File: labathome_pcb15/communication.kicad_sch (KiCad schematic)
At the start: 19 parts, among them M1 W5500_mini, SW2 OFF TERM ON, SW3 TERM ON, U1 MAX3485, U15 NRF24L01, U6 RFM95W-868S2, U7 SN65HVD230, X3 SIM7080G

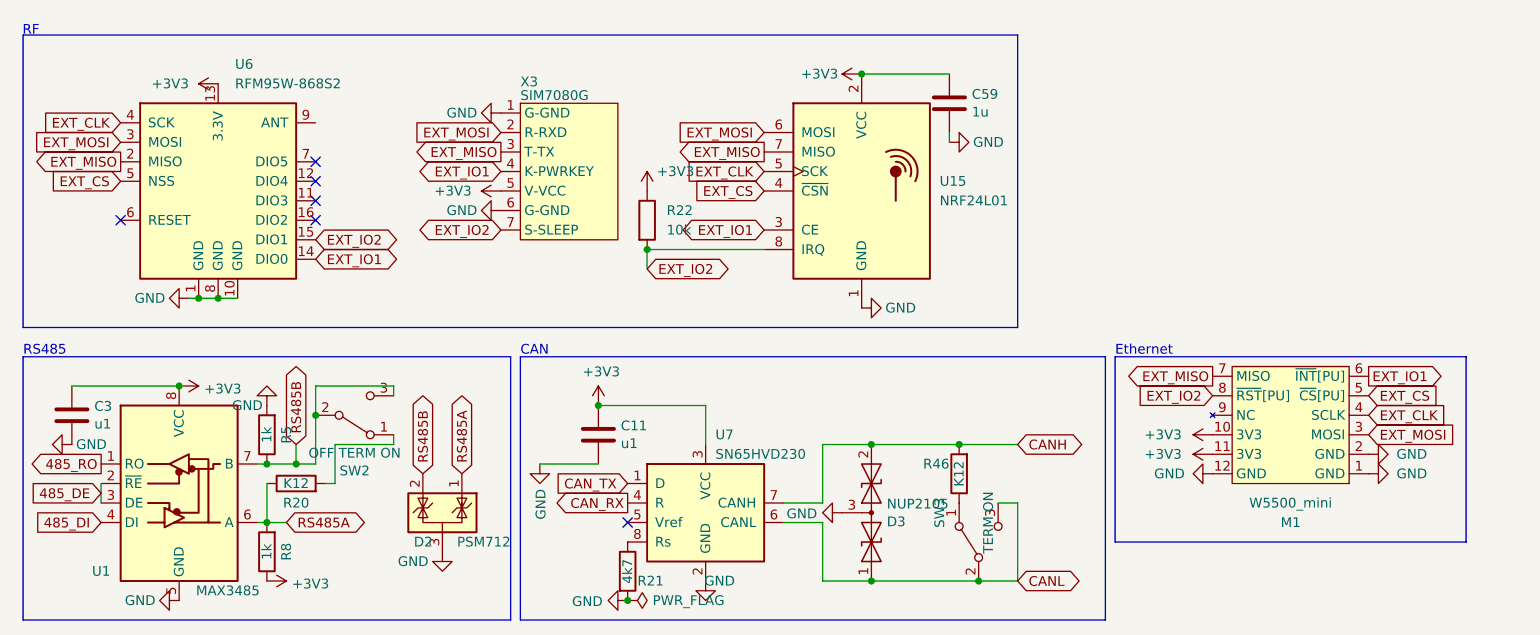
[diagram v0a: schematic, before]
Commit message: Various PCB and Code updates after review from Jana Marie Hemsing. Big Thankyou
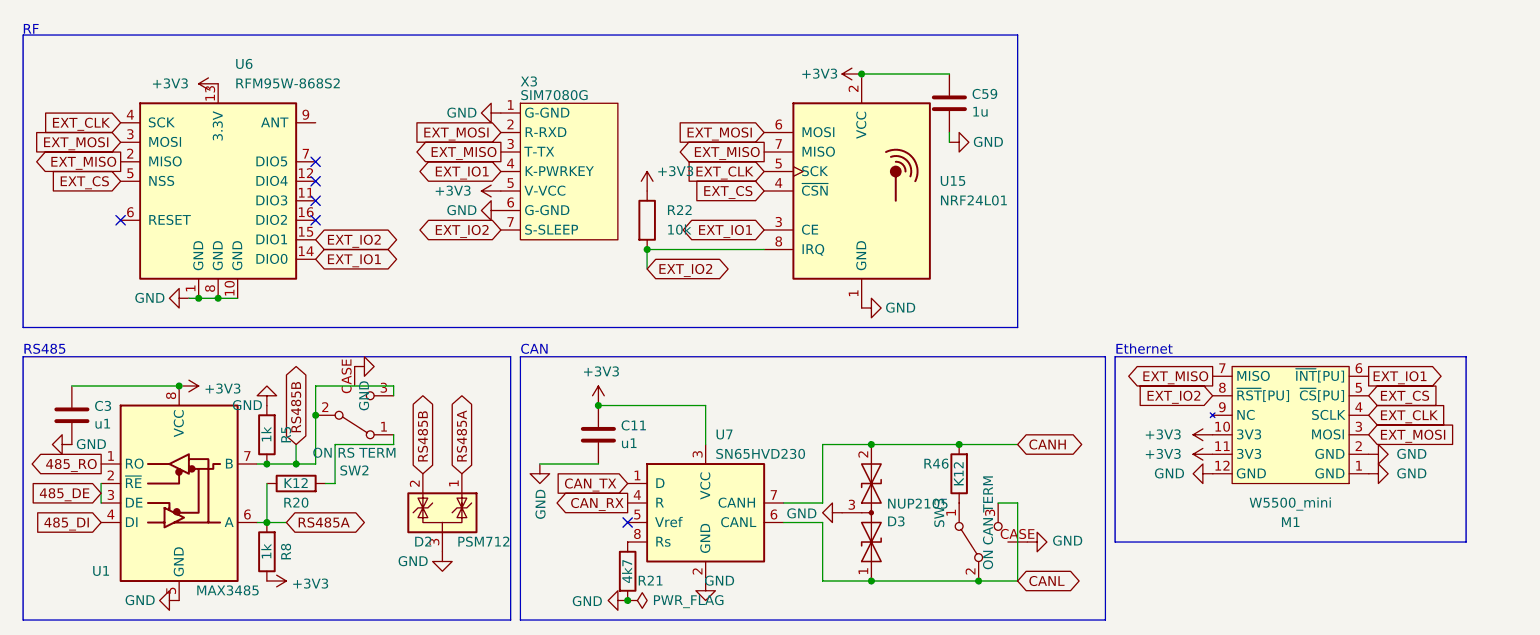
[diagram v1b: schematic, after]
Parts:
- SW2: value OFF TERM ON -> ON RS TERM; symbol Switch:SW_SPDT -> liebler_MECH:SW_SPDT_with_Case
- SW3: value TERM ON -> ON CAN TERM; symbol Switch:SW_SPDT -> liebler_MECH:SW_SPDT_with_Case
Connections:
- net GND: now also SW2.CASE, SW3.CASE
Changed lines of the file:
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@@
+	)
+	(symbol
+		(lib_id "power:GND")
+		(at 144.78 82.55 90)
+		(unit 1)
+		(exclude_from_sim no)
+		(in_bom yes)
+		(on_board yes)
+		(dnp no)
+		(property "Reference" "#PWR0211"
+			(at 151.13 82.55 0)
+			(effects
+				(font
+					(size 1.27 1.27)
+				)
+				(hide yes)
+			)
+		)
+		(property "Value" "GND"
+			(at 148.0312 82.423 90)
+			(effects
+				(font
+					(size 1.27 1.27)
+				)
+				(justify right)
+			)
+		)
+		(property "Footprint" ""
+			(at 144.78 82.55 0)
+			(effects
+				(font
+					(size 1.27 1.27)
+				)
+				(hide yes)
+			)
+		)
+		(property "Datasheet" ""
+			(at 144.78 82.55 0)
+			(effects
+				(font
+					(size 1.27 1.27)
+				)
+				(hide yes)
+			)
+		)
+		(property "Description" ""
+			(at 144.78 82.55 0)
+			(effects
+				(font
+					(size 1.27 1.27)
+				)
+				(hide yes)
+			)
+		)
+		(pin "1"
+		)
+		(instances
+			(project "labathome_pcb15"
+				(path "/e4d6926a-1a8b-424d-97c4-66b6ad87e4ac/30ce59dc-c3cd-4018-ad35-6ea0c32a1935"
+					(reference "#PWR0211")
+					(unit 1)
+				)
+			)
+		)
 	)
 	(symbol
@@
 	)
 	(symbol
-		(lib_id "Switch:SW_SPDT")
+		(lib_id "liebler_MECH:SW_SPDT_with_Case")
 		(at 138.43 82.55 90)
 		(unit 1)
@@
 			)
 		)
-		(property "Value" "TERM ON"
+		(property "Value" "ON CAN TERM"
 			(at 139.7 80.01 0)
 			(effects
@@
 			)
 		)
-		(property "Description" ""
+		(property "Description" "Switch, single pole double throw"
 			(at 138.43 82.55 0)
 			(effects
@@
 		(pin "3"
 		)
+		(pin "CASE"
+		)
 		(instances
 			(project "labathome_pcb15"
 				(path "/e4d6926a-1a8b-424d-97c4-66b6ad87e4ac/30ce59dc-c3cd-4018-ad35-6ea0c32a1935"
 					(reference "SW3")
+					(unit 1)
+				)
+			)
+		)
+	)
+	(symbol
+		(lib_id "power:GND")
+		(at 57.15 59.69 90)
+		(unit 1)
+		(exclude_from_sim no)
+		(in_bom yes)
+		(on_board yes)
+		(dnp no)
+		(property "Reference" "#PWR0213"
+			(at 63.5 59.69 0)
+			(effects
+				(font
+					(size 1.27 1.27)
+				)
+				(hide yes)
+			)
+		)
+		(property "Value" "GND"
+			(at 58.42 63.5 0)
+			(effects
+				(font
+					(size 1.27 1.27)
+				)
+			)
+		)
+		(property "Footprint" ""
+			(at 57.15 59.69 0)
+			(effects
+				(font
+					(size 1.27 1.27)
+				)
+				(hide yes)
+			)
+		)
+		(property "Datasheet" ""
+			(at 57.15 59.69 0)
+			(effects
+				(font
+					(size 1.27 1.27)
+				)
+				(hide yes)
+			)
+		)
+		(property "Description" ""
+			(at 57.15 59.69 0)
+			(effects
+				(font
+					(size 1.27 1.27)
+				)
+				(hide yes)
+			)
+		)
+		(pin "1"
+		)
+		(instances
+			(project "labathome_pcb15"
+				(path "/e4d6926a-1a8b-424d-97c4-66b6ad87e4ac/30ce59dc-c3cd-4018-ad35-6ea0c32a1935"
+					(reference "#PWR0213")
 					(unit 1)
 				)
@@
 	)
 	(symbol
-		(lib_id "Switch:SW_SPDT")
+		(lib_id "liebler_MECH:SW_SPDT_with_Case")
 		(at 57.15 66.04 0)
 		(mirror x)
@@
 			)
 		)
-		(property "Value" "OFF TERM  ON"
+		(property "Value" "ON RS TERM"
 			(at 57.15 70.9676 0)
 			(effects
@@
 			)
 		)
-		(property "Description" ""
+		(property "Description" "Switch, single pole double throw"
 			(at 57.15 66.04 0)
 			(effects
@@
 		(pin "3"
 		)
-		(instances
+		(pin "CASE"
+		)
+		(instances

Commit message: Further improventents in PCB layout
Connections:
- no-connect marks 6 -> 7
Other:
- moved on the sheet: C3

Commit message: Updates in PCB, arduino test firmware
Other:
- note added: "RF (mutual exclusive, only place one!)"
- note removed: "RF"
- company: (none) -> Klaus Liebler
- title: (none) -> lab@home
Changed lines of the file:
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@@
 	(generator_version "8.0")
 	(paper "A4")
+	(title_block
+		(title "lab@home")
+		(date "2024-08-19")
+		(rev "15.1")
+		(company "Klaus Liebler")
+	)
 	(junction
 		(at 138.43 87.63)
@@
 		)
 	)
-	(text "RF"
+	(text "RF (mutual exclusive, only place one!)"
 		(exclude_from_sim no)
-		(at 14.986 16.002 0)
+		(at 13.716 16.256 0)
 		(effects
 			(font
 				(size 1.27 1.27)
 			)
-		)
-	)
+			(justify left bottom)
+		)
+	)

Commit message: Various last minute
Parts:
- C11, C3: footprint Capacitor_SMD:C_0402_1005Metric -> Capacitor_SMD:C_0201_0603Metric
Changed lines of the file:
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@@
 			)
 		)
-		(property "Footprint" "Capacitor_SMD:C_0402_1005Metric"
+		(property "Footprint" "Capacitor_SMD:C_0201_0603Metric"
 			(at 19.3548 59.69 0)
 			(effects
@@
 			)
 		)
-		(property "Footprint" "Capacitor_SMD:C_0402_1005Metric"
+		(property "Footprint" "Capacitor_SMD:C_0201_0603Metric"
 			(at 89.8652 72.39 0)
 			(effects

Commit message: 4 Layers
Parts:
- R21: value 4k7 -> 10k; footprint Resistor_SMD:R_0402_1005Metric -> Resistor_SMD:R_0201_0603Metric
- R22: footprint Resistor_SMD:R_0402_1005Metric -> Resistor_SMD:R_0201_0603Metric
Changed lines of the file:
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@@
 			)
 		)
-		(property "Value" "4k7"
+		(property "Value" "10k"
 			(at 92.71 86.36 90)
 			(effects
@@
 			)
 		)
-		(property "Footprint" "Resistor_SMD:R_0402_1005Metric"
+		(property "Footprint" "Resistor_SMD:R_0201_0603Metric"
 			(at 90.932 86.36 90)
 			(effects
@@
 			)
 		)
-		(property "Footprint" "Resistor_SMD:R_0402_1005Metric"
+		(property "Footprint" "Resistor_SMD:R_0201_0603Metric"
 			(at 93.472 40.64 90)
 			(effects

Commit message: Minimal changes
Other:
- note removed: "Ethernet"
- moved on the sheet: M1
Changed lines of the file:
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@@
 		)
 	)
-	(polyline
-		(pts
-			(xy 156.21 58.42) (xy 156.21 82.55)
-		)
-		(stroke
-			(width 0)
-			(type default)
-		)
-	)
 	(wire
 		(pts
@@
 		)
 	)
-	(polyline
-		(pts
-			(xy 156.21 58.42) (xy 201.93 58.42)
-		)
-		(stroke
-			(width 0)
-			(type default)
-		)
-	)
 	(wire
 		(pts
@@
 		)
 	)
-	(polyline
-		(pts
-			(xy 201.93 82.55) (xy 156.21 82.55)
-		)
-		(stroke
-			(width 0)
-			(type default)
-		)
-	)
 	(wire
 		(pts
@@
 		)
 	)
-	(polyline
-		(pts
-			(xy 201.93 58.42) (xy 201.93 82.55)
-		)
-		(stroke
-			(width 0)
-			(type default)
-		)
-	)
 	(wire
 		(pts
@@
 	(rectangle
 		(start 13.97 16.51)
-		(end 143.51 54.61)
+		(end 209.55 54.61)
 		(stroke
 			(width 0)
@@
 		)
 	)
-	(text "Ethernet\n"
-		(exclude_from_sim no)
-		(at 156.21 58.42 0)
-		(effects
-			(font
-				(size 1.27 1.27)
-			)
-			(justify left bottom)
-		)
-	)
 	(text "CAN"
 		(exclude_from_sim no)
@@
 	(global_label "EXT_MISO"
 		(shape output)
-		(at 168.91 60.96 180)
+		(at 162.56 25.4 180)
 		(fields_autoplaced yes)
 		(effects
@@
 		)
 		(property "Intersheetrefs" "${INTERSHEET_REFS}"
-			(at 157.0349 60.96 0)
+			(at 150.6849 25.4 0)
 			(effects
 				(font
@@
 	(global_label "EXT_IO1"
 		(shape output)
-		(at 189.23 60.96 0)
+		(at 182.88 25.4 0)
 		(fields_autoplaced yes)
 		(effects
@@
 		)
 		(property "Intersheetrefs" "${INTERSHEET_REFS}"
-			(at 199.6537 60.96 0)
+			(at 193.3037 25.4 0)
 			(effects
 				(font
@@
 	(global_label "EXT_CS"
 		(shape input)
-		(at 189.23 63.5 0)
+		(at 182.88 27.94 0)
 		(fields_autoplaced yes)
 		(effects
@@
 		)
 		(property "Intersheetrefs" "${INTERSHEET_REFS}"
-			(at 198.9884 63.5 0)
+			(at 192.6384 27.94 0)
 			(effects
 				(font
@@
 	(global_label "EXT_MOSI"
 		(shape input)
-		(at 189.23 68.58 0)
+		(at 182.88 33.02 0)
 		(fields_autoplaced yes)
 		(effects
@@
 		)
 		(property "Intersheetrefs" "${INTERSHEET_REFS}"
-			(at 201.1051 68.58 0)
+			(at 194.7551 33.02 0)
 			(effects
 				(font
@@
 	(global_label "EXT_CLK"
 		(shape input)
-		(at 189.23 66.04 0)
+		(at 182.88 30.48 0)
 		(fields_autoplaced yes)
 		(effects
@@
 		)
 		(property "Intersheetrefs" "${INTERSHEET_REFS}"
-			(at 200.077 66.04 0)
+			(at 193.727 30.48 0)
 			(effects
 				(font
@@
 	(global_label "EXT_IO2"
 		(shape input)
-		(at 168.91 63.5 180)
+		(at 162.56 27.94 180)
 		(fields_autoplaced yes)
 		(effects
@@
 		)
 		(property "Intersheetrefs" "${INTERSHEET_REFS}"
-			(at 158.4863 63.5 0)
+			(at 152.1363 27.94 0)
 			(effects
 				(font
@@
 	(symbol
 		(lib_id "power:+3V3")
-		(at 168.91 68.58 90)
+		(at 162.56 33.02 90)
 		(unit 1)
 		(exclude_from_sim no)
@@
 		(dnp no)
 		(property "Reference" "#PWR0157"
-			(at 172.72 68.58 0)
+			(at 166.37 33.02 0)
 			(effects
 				(font
@@
 		)
 		(property "Value" "+3V3"
-			(at 160.02 68.58 90)
+			(at 153.67 33.02 90)
 			(effects
 				(font
@@
 		)
 		(property "Footprint" ""
-			(at 168.91 68.58 0)
+			(at 162.56 33.02 0)
 			(effects
 				(font
@@
 		)
 		(property "Datasheet" ""
-			(at 168.91 68.58 0)
+			(at 162.56 33.02 0)
 			(effects
 				(font
@@
 		)
 		(property "Description" "Power symbol creates a global label with name \"+3V3\""
-			(at 168.91 68.58 0)
+			(at 162.56 33.02 0)
 			(effects
 				(font
@@
 	(symbol
 		(lib_id "power:+3V3")
-		(at 168.91 71.12 90)
+		(at 162.56 35.56 90)
 		(unit 1)
 		(exclude_from_sim no)
@@
 		(dnp no)
 		(property "Reference" "#PWR0158"
-			(at 172.72 71.12 0)
+			(at 166.37 35.56 0)
 			(effects
 				(font
@@
 		)
 		(property "Value" "+3V3"
-			(at 160.02 71.12 90)
+			(at 153.67 35.56 90)
 			(effects
 				(font
@@
 		)
 		(property "Footprint" ""
-			(at 168.91 71.12 0)
+			(at 162.56 35.56 0)
 			(effects
 				(font
@@
 		)
 		(property "Datasheet" ""
-			(at 168.91 71.12 0)
+			(at 162.56 35.56 0)
 			(effects
 				(font
@@
 		)
 		(property "Description" "Power symbol creates a global label with name \"+3V3\""
-			(at 168.91 71.12 0)
+			(at 162.56 35.56 0)
 			(effects
 				(font
@@
 	(symbol
 		(lib_id "power:GND")
-		(at 189.23 73.66 90)
+		(at 182.88 38.1 90)
 		(unit 1)
 		(exclude_from_sim no)
@@
 		(dnp no)
 		(property "Reference" "#PWR0195"
-			(at 195.58 73.66 0)
+			(at 189.23 38.1 0)
 			(effects
 				(font
@@
 		)
 		(property "Value" "GND"
-			(at 196.85 73.66 90)
+			(at 190.5 38.1 90)
 			(effects
 				(font
@@
 		)
 		(property "Footprint" ""
-			(at 189.23 73.66 0)
+			(at 182.88 38.1 0)
 			(effects
 				(font
@@
 		)
 		(property "Datasheet" ""
-			(at 189.23 73.66 0)
+			(at 182.88 38.1 0)
 			(effects
 				(font
@@
 		)
 		(property "Description" "Power symbol creates a global label with name \"GND\" , ground"
-			(at 189.23 73.66 0)
+			(at 182.88 38.1 0)
 			(effects
 				(font
@@
 	(symbol
 		(lib_id "power:GND")
-		(at 189.23 71.12 90)
+		(at 182.88 35.56 90)
 		(unit 1)
 		(exclude_from_sim no)
@@
 		(dnp no)
 		(property "Reference" "#PWR0162"
-			(at 195.58 71.12 0)
+			(at 189.23 35.56 0)
 			(effects
 				(font
@@
 		)
 		(property "Value" "GND"
-			(at 196.85 71.12 90)
+			(at 190.5 35.56 90)
 			(effects
 				(font
@@
 		)
 		(property "Footprint" ""
-			(at 189.23 71.12 0)
+			(at 182.88 35.56 0)
 			(effects
 				(font
@@
 		)
 		(property "Datasheet" ""
-			(at 189.23 71.12 0)
+			(at 182.88 35.56 0)
 			(effects
 				(font
@@
 		)
 		(property "Description" "Power symbol creates a global label with name \"GND\" , ground"
-			(at 189.23 71.12 0)
+			(at 182.88 35.56 0)
 			(effects
 				(font
@@
 	(symbol
 		(lib_id "liebler_MODULES:W5500_mini")
-		(at 179.07 67.31 180)
+		(at 172.72 31.75 180)
 		(unit 1)
 		(exclude_from_sim no)
@@
 		(fields_autoplaced yes)
 		(property "Reference" "M1"
-			(at 179.07 80.01 0)
+			(at 172.72 44.45 0)
 			(effects
 				(font
@@
 		)
 		(property "Value" "W5500_mini"
-			(at 179.07 77.47 0)
+			(at 172.72 41.91 0)
 			(effects
 				(font
@@
 		)
 		(property "Footprint" "liebler_MODULES:W5500-mini"
-			(at 179.07 67.31 0)
+			(at 172.72 31.75 0)
 			(effects
 				(font
@@
 		)
 		(property "Datasheet" ""
-			(at 179.07 67.31 0)
+			(at 172.72 31.75 0)
 			(effects
 				(font
@@
 		)
 		(property "Description" ""
-			(at 179.07 67.31 0)
+			(at 172.72 31.75 0)
 			(effects
 				(font
@@
 	(symbol
 		(lib_id "power:GND")
-		(at 168.91 73.66 270)
+		(at 162.56 38.1 270)
 		(unit 1)
 		(exclude_from_sim no)
@@
 		(dnp no)
 		(property "Reference" "#PWR0161"
-			(at 162.56 73.66 0)
+			(at 156.21 38.1 0)
 			(effects
 				(font
@@
 		)
 		(property "Value" "GND"
-			(at 161.29 73.66 90)
+			(at 154.94 38.1 90)
 			(effects
 				(font
@@
 		)
 		(property "Footprint" ""
-			(at 168.91 73.66 0)
+			(at 162.56 38.1 0)
 			(effects
 				(font
@@
 		)
 		(property "Datasheet" ""
-			(at 168.91 73.66 0)
+			(at 162.56 38.1 0)
 			(effects
 				(font
@@
 		)
 		(property "Description" "Power symbol creates a global label with name \"GND\" , ground"
-			(at 168.91 73.66 0)
+			(at 162.56 38.1 0)
 			(effects
 				(font

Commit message: IP5306
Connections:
- net RS485A: now also D2.2 (K); no longer D2.1 (K)
- net RS485B: now also D2.1 (K); no longer D2.2 (K)
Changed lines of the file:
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@@
 		(lib_id "Power_Protection:NUP2105L")
 		(at 68.58 78.74 0)
-		(mirror y)
 		(unit 1)
 		(exclude_from_sim no)
@@
 		(dnp no)
 		(property "Reference" "D2"
-			(at 67.31 82.55 0)
+			(at 69.85 82.55 0)
 			(effects
 				(font
@@
 		)
 		(property "Value" "PSM712"
-			(at 77.47 82.55 0)
+			(at 59.69 82.55 0)
 			(effects
 				(font
@@
 		)
 		(property "Footprint" "Package_TO_SOT_SMD:SOT-23_Handsoldering"
-			(at 62.865 80.01 0)
+			(at 74.295 80.01 0)
 			(effects
 				(font
@@
 		)
 		(property "Datasheet" "https://www.onsemi.com/pub_link/Collateral/NUP2105L-D.PDF"
-			(at 65.405 75.565 0)
+			(at 71.755 75.565 0)
 			(effects
 				(font

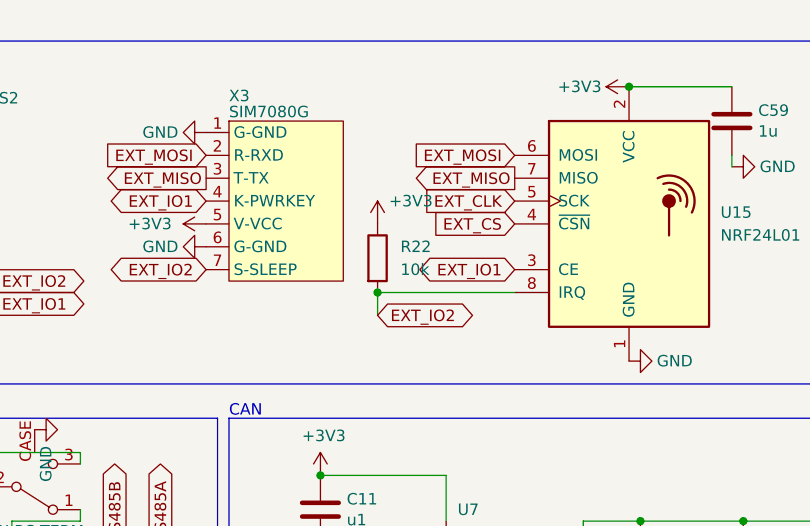
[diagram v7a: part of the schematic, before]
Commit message: Added stepper, no DRC errors, not yet optimized
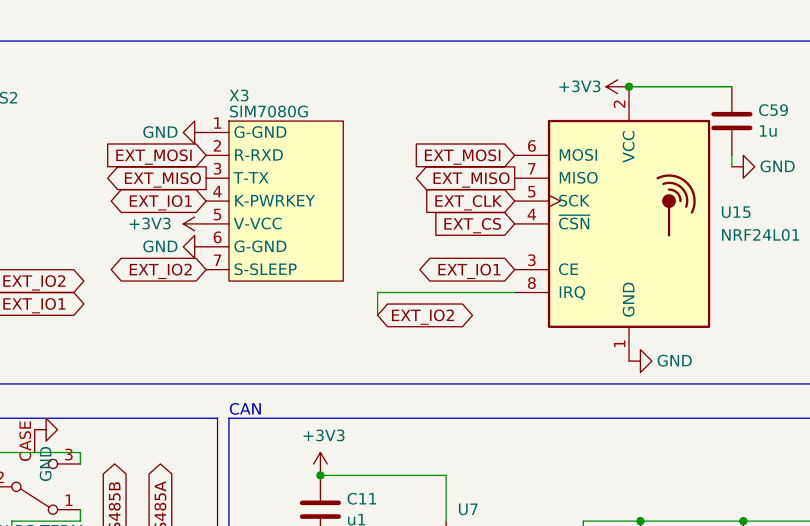
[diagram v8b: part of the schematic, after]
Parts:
- removed R22: 10k, Resistor_SMD:R_0201_0603Metric, symbol Device:R
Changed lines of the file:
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@@
 	)
 	(junction
-		(at 95.25 44.45)
-		(diameter 0)
-		(color 0 0 0 0)
-	)
-	(junction
 		(at 52.07 66.04)
 		(diameter 0)
@@
 	)
 	(symbol
-		(lib_id "power:+3V3")
-		(at 95.25 36.83 0)
-		(unit 1)
-		(exclude_from_sim no)
-		(in_bom yes)
-		(on_board yes)
-		(dnp no)
-		(property "Reference" "#PWR047"
-			(at 95.25 40.64 0)
-			(effects
-				(font
-					(size 1.27 1.27)
-				)
-				(hide yes)
-			)
-		)
-		(property "Value" "+3V3"
-			(at 96.52 34.29 0)
-			(effects
-				(font
-					(size 1.27 1.27)
-				)
-				(justify left)
-			)
-		)
-		(property "Footprint" ""
-			(at 95.25 36.83 0)
-			(effects
-				(font
-					(size 1.27 1.27)
-				)
-				(hide yes)
-			)
-		)
-		(property "Datasheet" ""
-			(at 95.25 36.83 0)
-			(effects
-				(font
-					(size 1.27 1.27)
-				)
-				(hide yes)
-			)
-		)
-		(property "Description" "Power symbol creates a global label with name \"+3V3\""
-			(at 95.25 36.83 0)
-			(effects
-				(font
-					(size 1.27 1.27)
-				)
-				(hide yes)
-			)
-		)
-		(pin "1"
-		)
-		(instances
-			(project "labathome_pcb15"
-				(path "/e4d6926a-1a8b-424d-97c4-66b6ad87e4ac/30ce59dc-c3cd-4018-ad35-6ea0c32a1935"
-					(reference "#PWR047")
-					(unit 1)
-				)
-			)
-		)
-	)
-	(symbol
 		(lib_id "Device:R")
 		(at 92.71 86.36 0)
@@
 					(unit 1)
 				)
-			)
-		)
-	)
-	(symbol
-		(lib_id "Device:R")
-		(at 95.25 40.64 0)
-		(unit 1)
-		(exclude_from_sim no)
-		(in_bom yes)
-		(on_board yes)
-		(dnp no)
-		(fields_autoplaced yes)
-		(property "Reference" "R22"
-			(at 97.79 39.3699 0)
-			(effects
-				(font
-					(size 1.27 1.27)
-				)
-				(justify left)
-			)
-		)
-		(property "Value" "10k"
-			(at 97.79 41.9099 0)
-			(effects
-				(font
-					(size 1.27 1.27)
-				)
-				(justify left)
-			)
-		)
-		(property "Footprint" "Resistor_SMD:R_0201_0603Metric"
-			(at 93.472 40.64 90)
-			(effects
-				(font
-					(size 1.27 1.27)
-				)
-				(hide yes)
-			)
-		)
-		(property "Datasheet" "~"
-			(at 95.25 40.64 0)
-			(effects
-				(font
-					(size 1.27 1.27)
-				)
-				(hide yes)
-			)
-		)
-		(property "Description" ""
-			(at 95.25 40.64 0)
-			(effects
-				(font
-					(size 1.27 1.27)
-				)
-				(hide yes)
-			)
-		)
-		(pin "1"
-		)
-		(pin "2"
-		)
-		(instances
-			(project "labathome_pcb15"
-				(path "/e4d6926a-1a8b-424d-97c4-66b6ad87e4ac/30ce59dc-c3cd-4018-ad35-6ea0c32a1935"
-					(reference "R22")
-					(unit 1)
-				)
